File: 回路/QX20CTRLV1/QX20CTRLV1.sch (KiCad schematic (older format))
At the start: 38 parts, among them J1 VH_CAN, J10 PA1, J11 PA2, J12 PA3, J13 PA4, J14 SWDIO, J15 SWDCLK, J16 3.3V, J2 VH_CAN, J3 VH_SRV1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

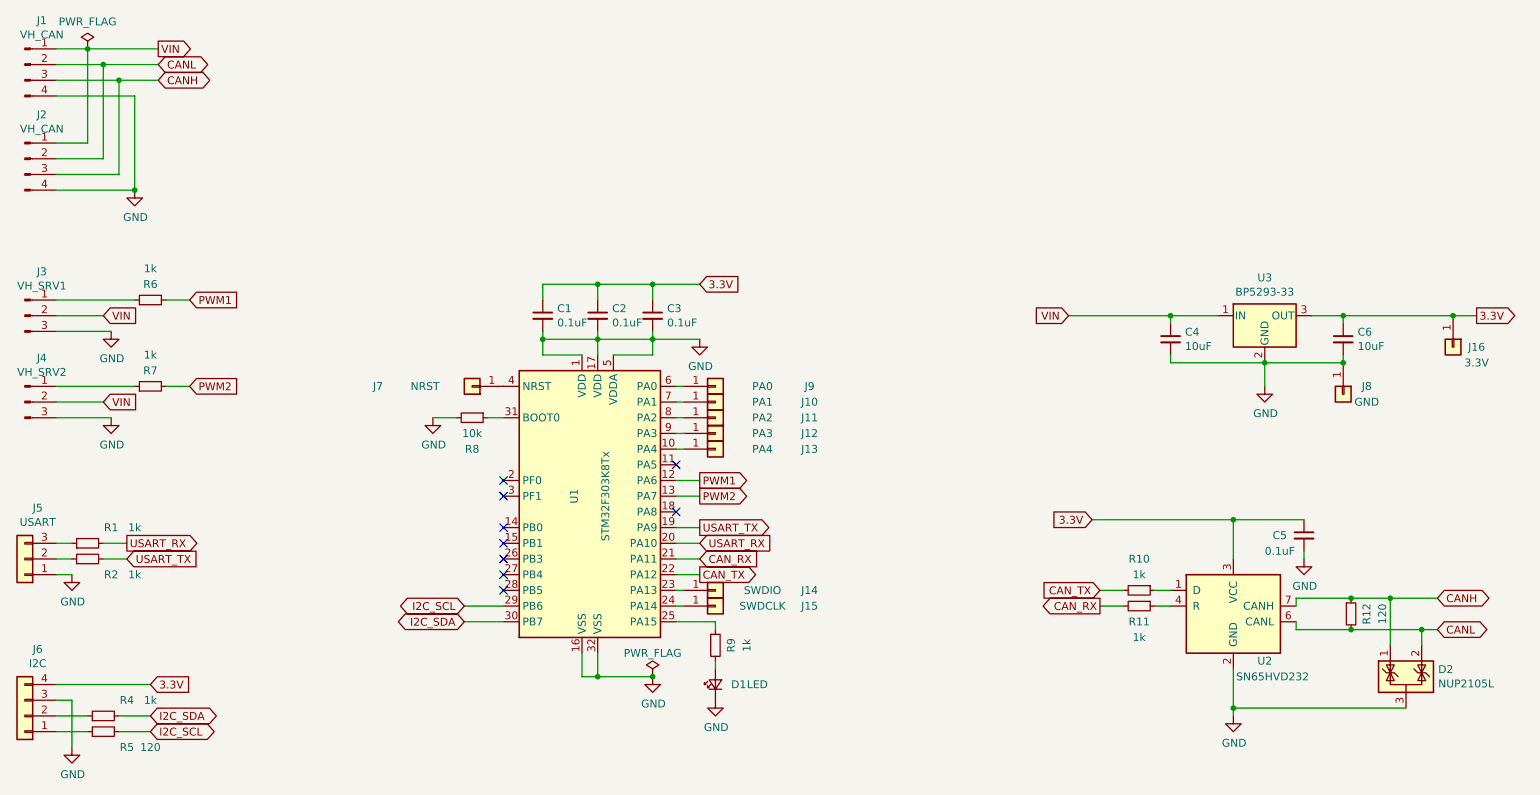
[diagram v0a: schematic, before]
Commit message: QX20CTRLV2
QX20コントローラーV2　NC基板用
回路図、実装図、ガーバーデータまで。
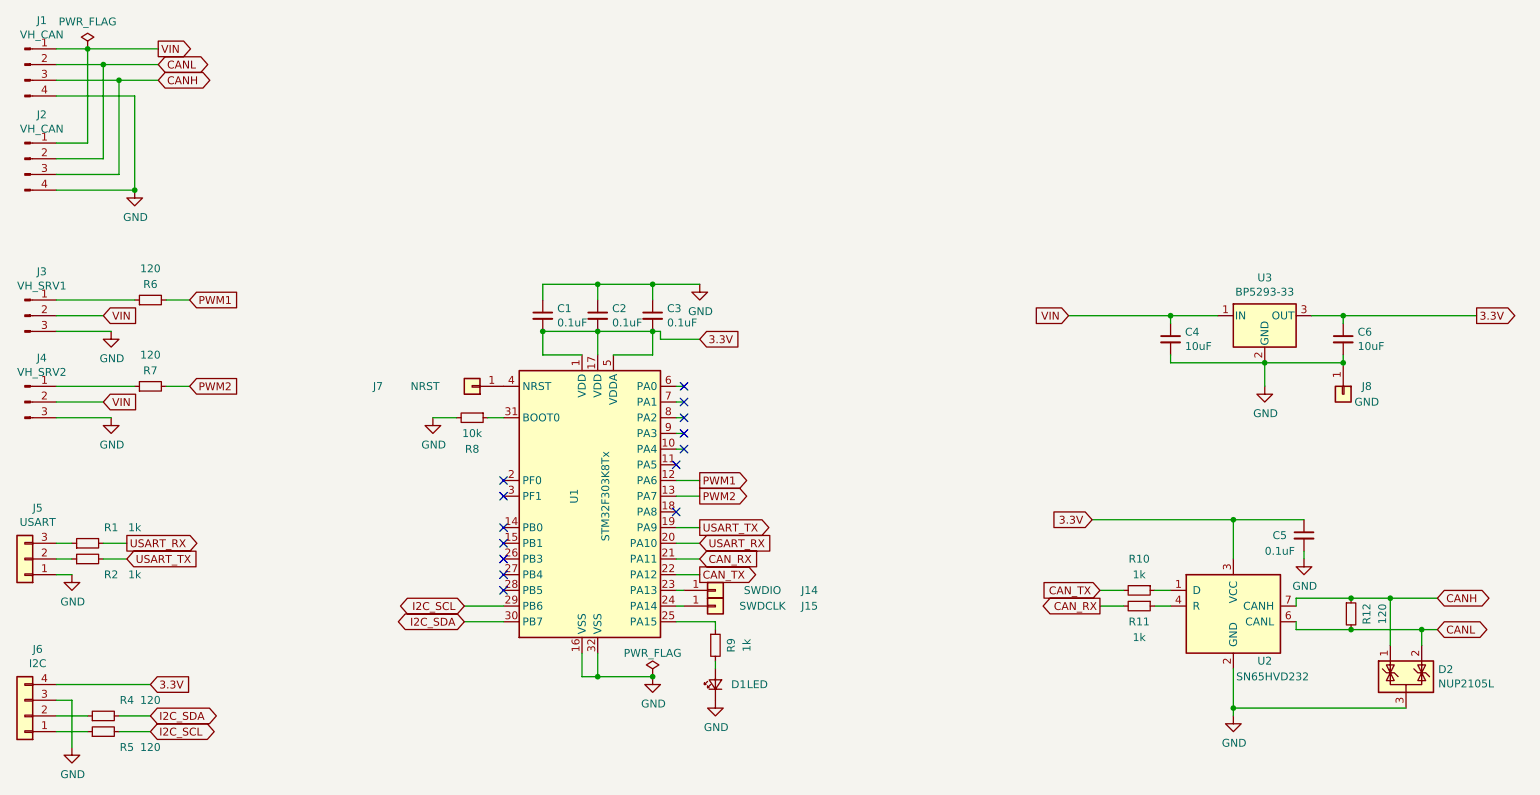
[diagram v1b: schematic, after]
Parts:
- removed J10: PA1, Connector_Pin:Pin_D1.3mm_L11.0mm, symbol Connector_Generic:Conn_01x01
- removed J11: PA2, Connector_Pin:Pin_D1.3mm_L11.0mm, symbol Connector_Generic:Conn_01x01
- removed J12: PA3, Connector_Pin:Pin_D1.3mm_L11.0mm, symbol Connector_Generic:Conn_01x01
- removed J13: PA4, Connector_Pin:Pin_D1.3mm_L11.0mm, symbol Connector_Generic:Conn_01x01
- removed J16: 3.3V, Connector_Pin:Pin_D1.3mm_L11.0mm, symbol Connector_Generic:Conn_01x01
- removed J9: PA0, Connector_Pin:Pin_D1.3mm_L11.0mm, symbol Connector_Generic:Conn_01x01
- C1, C2, C3, C4, C5, C6: footprint Diode_SMD:D_0805_2012Metric_Pad1.15x1.40mm_HandSolder -> Capacitor_SMD:C_1206_3216Metric_Pad1.42x1.75mm_HandSolder
- J14, J15, J7, J8: footprint Connector_Pin:Pin_D1.3mm_L11.0mm -> Connector_Wire:SolderWirePad_1x01_Drill1mm
- J5: footprint Connector_PinHeader_2.54mm:PinHeader_1x03_P2.54mm_Vertical -> Connector_PinSocket_2.54mm:PinSocket_1x03_P2.54mm_Vertical
- J6: footprint Connector_PinHeader_2.54mm:PinHeader_1x04_P2.54mm_Vertical -> Connector_PinSocket_2.54mm:PinSocket_1x04_P2.54mm_Vertical
- R4, R6, R7: value 1k -> 120
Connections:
- net 3.3V: now also C1.2, C2.2, C3.2, U1.1 (VDD), U1.17 (VDD), U1.5 (VDDA); no longer C1.1, C2.1, C3.1
- net GND: now also C1.1, C2.1, C3.1; no longer C1.2, C2.2, C3.2, U1.1 (VDD), U1.17 (VDD), U1.5 (VDDA)
- no-connect marks 9 -> 14
